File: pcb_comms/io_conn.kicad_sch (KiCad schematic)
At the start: 23 parts, among them IC1 CP2102N-A02-GQFN28, J1 Conn_01x06_Pin, J2 USB_B_Micro, J3 OBC_I2C, J5 OBC_I2C, J6 OBC_I2C, U6 ADP122AUJZ-3.3-R7

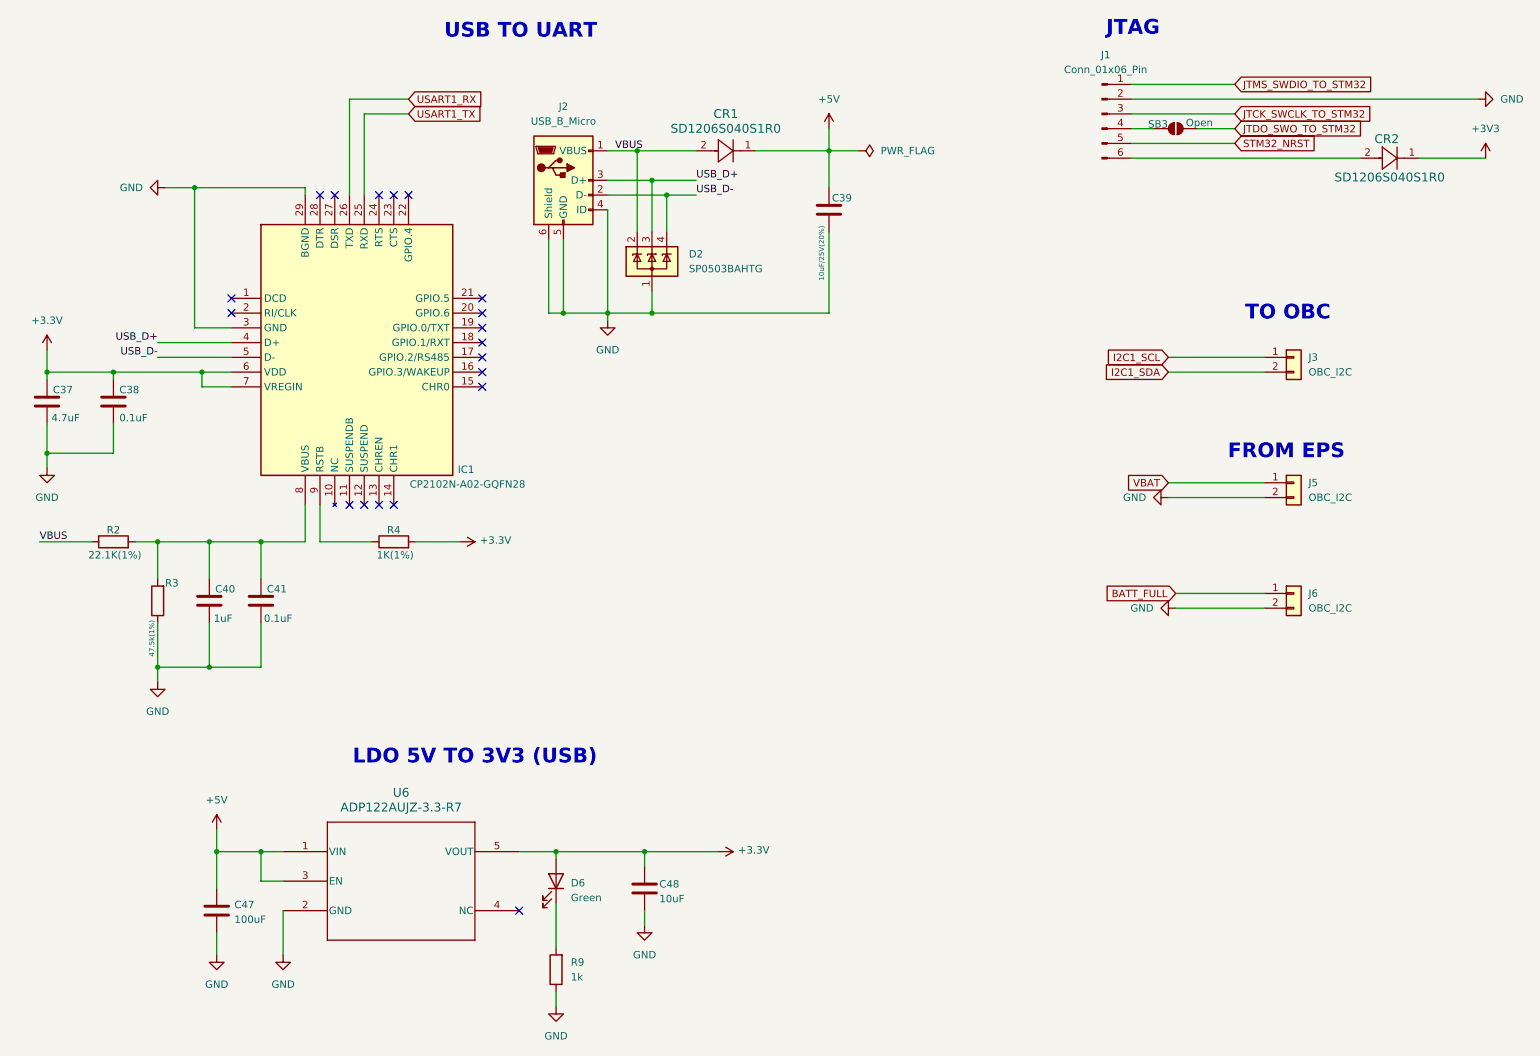
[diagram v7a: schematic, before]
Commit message: Finish schematic
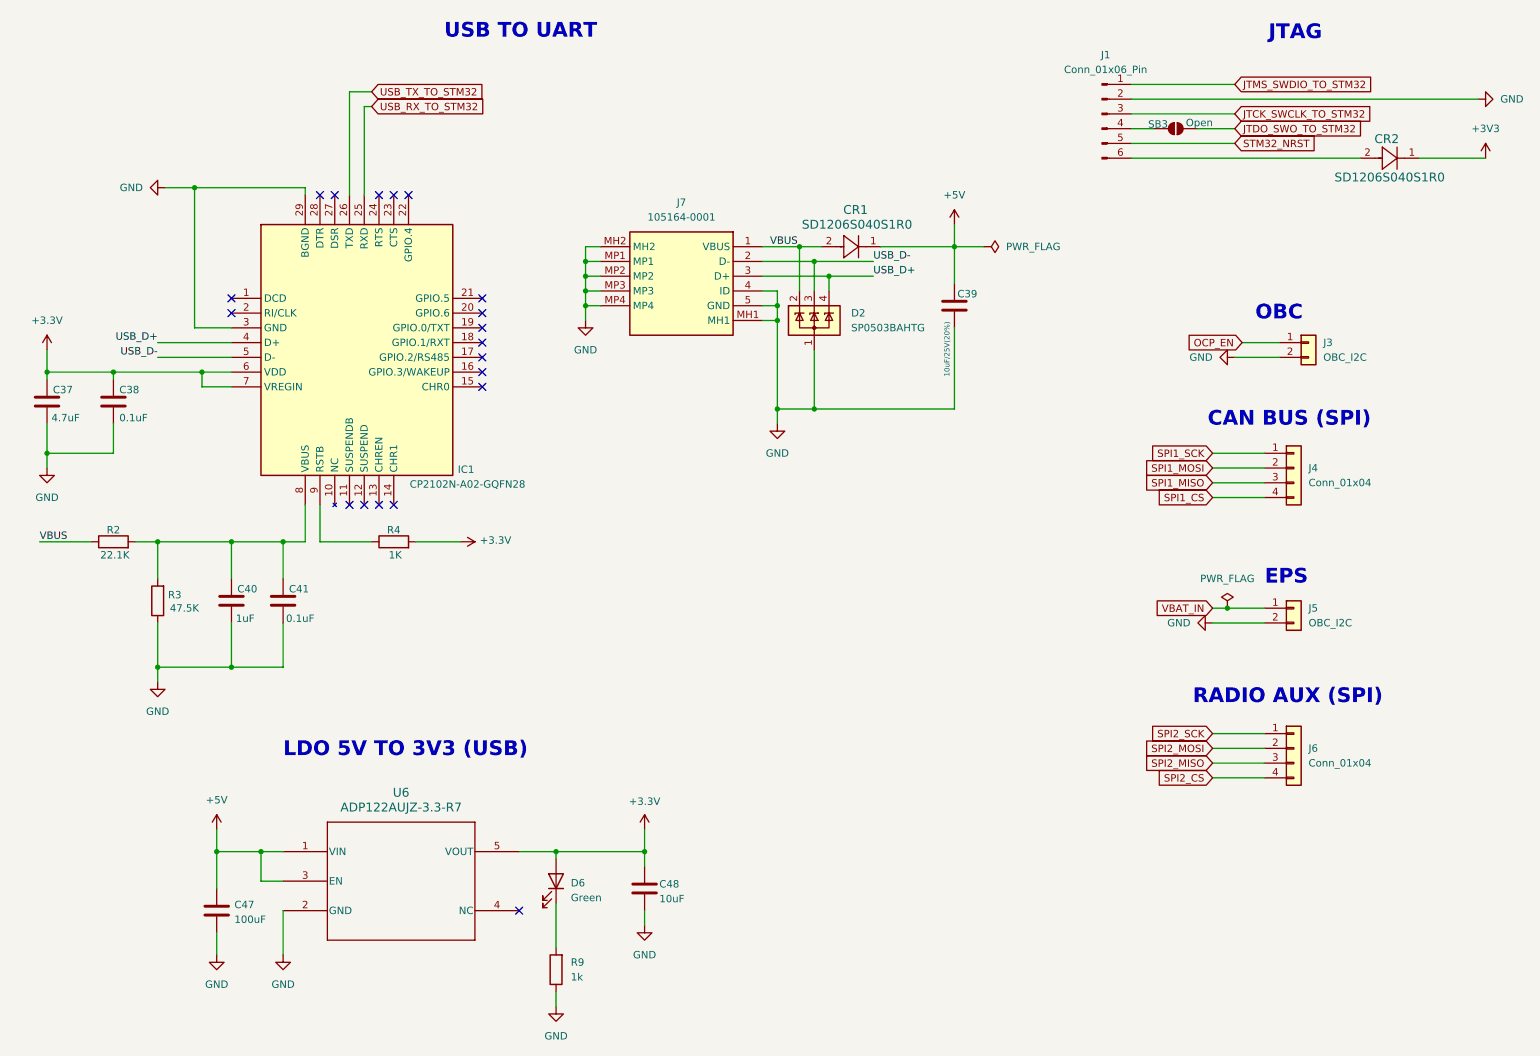
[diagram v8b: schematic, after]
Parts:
- removed J2: USB_B_Micro, symbol Connector:USB_B_Micro
- removed J6: OBC_I2C, symbol Connector_Generic:Conn_01x02
- added J4, J6: Conn_01x04, symbol Connector_Generic:Conn_01x04
- added J7: 105164-0001, symbol USB_RECEPTACLE_105164-0001:105164-0001
- R2: value 22.1K(1%) -> 22.1K
- R3: value 47.5k(1%) -> 47.5K
- R4: value 1K(1%) -> 1K
- U6: footprint ADP122AUJZ_3_3_R7:UJ_5_ADI -> (none)
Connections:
- net I2C1_SDA is gone; now on net GND: J3.2 (Pin_2)
- net GND: now also J7.4 (ID), J7.5 (GND), J7.MH1, J7.MH2, J7.MP1, J7.MP2, J7.MP3, J7.MP4
- net USB_D+: now also D2.4 (K), J7.3 (D+); no longer D2.3 (K)
- net USB_D-: now also D2.3 (K), J7.2 (D-); no longer D2.4 (K)
- net VBUS: now also J7.1 (VBUS)
- net I2C1_SCL renamed OCP_EN
- net USART1_RX renamed USB_TX_TO_STM32
- net USART1_TX renamed USB_RX_TO_STM32
- net VBAT renamed VBAT_IN
- new net SPI1_CS: J4.4 (Pin_4)
- new net SPI1_MISO: J4.3 (Pin_3)
- new net SPI1_MOSI: J4.2 (Pin_2)
- new net SPI1_SCK: J4.1 (Pin_1)
- new net SPI2_CS: J6.4 (Pin_4)
- new net SPI2_MISO: J6.3 (Pin_3)
- new net SPI2_MOSI: J6.2 (Pin_2)
- new net SPI2_SCK: J6.1 (Pin_1)
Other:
- note added: "CAN BUS (SPI)"
- note added: "EPS"
- note added: "OBC"
- note added: "RADIO AUX (SPI)"
- note removed: "FROM EPS"
- note removed: "TO OBC"
- moved on the sheet: C39, C40, C41, CR1, D2, J5
